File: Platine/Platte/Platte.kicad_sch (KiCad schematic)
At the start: 10 parts, among them J1 Conn_01x07_MountingPin, J2 Conn_01x04_Socket, J3 Conn_01x04_Socket

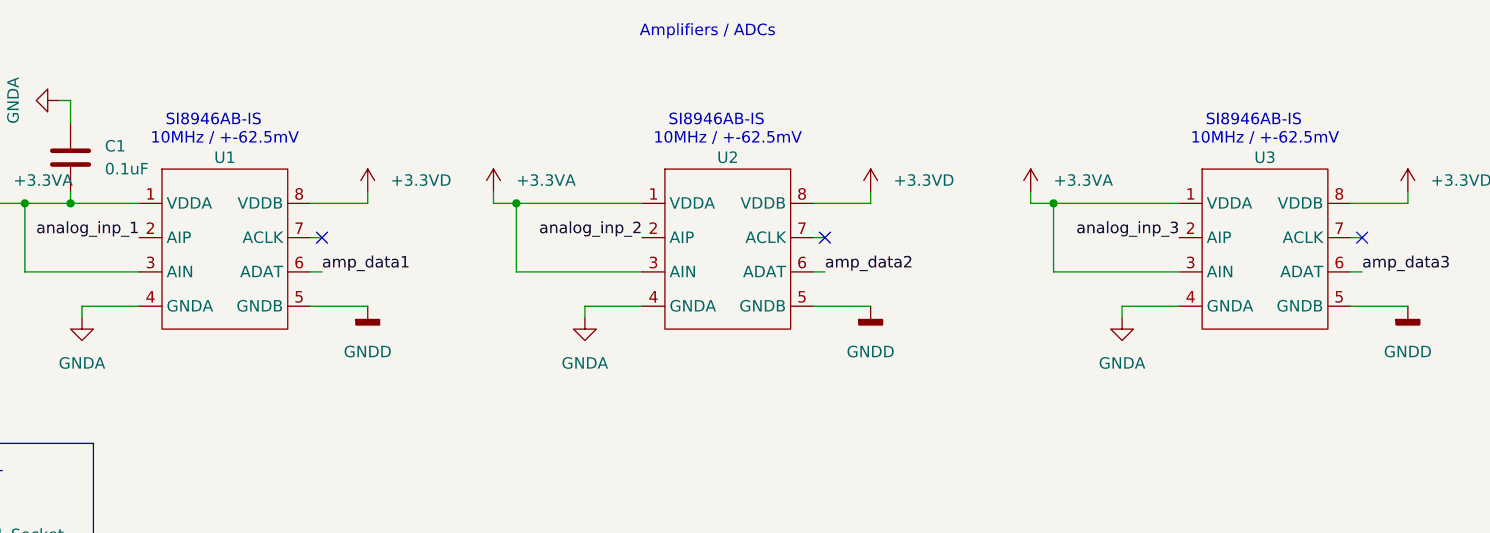
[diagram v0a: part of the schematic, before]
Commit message: Mit Robin geredet, ein paar Veränderung gemacht
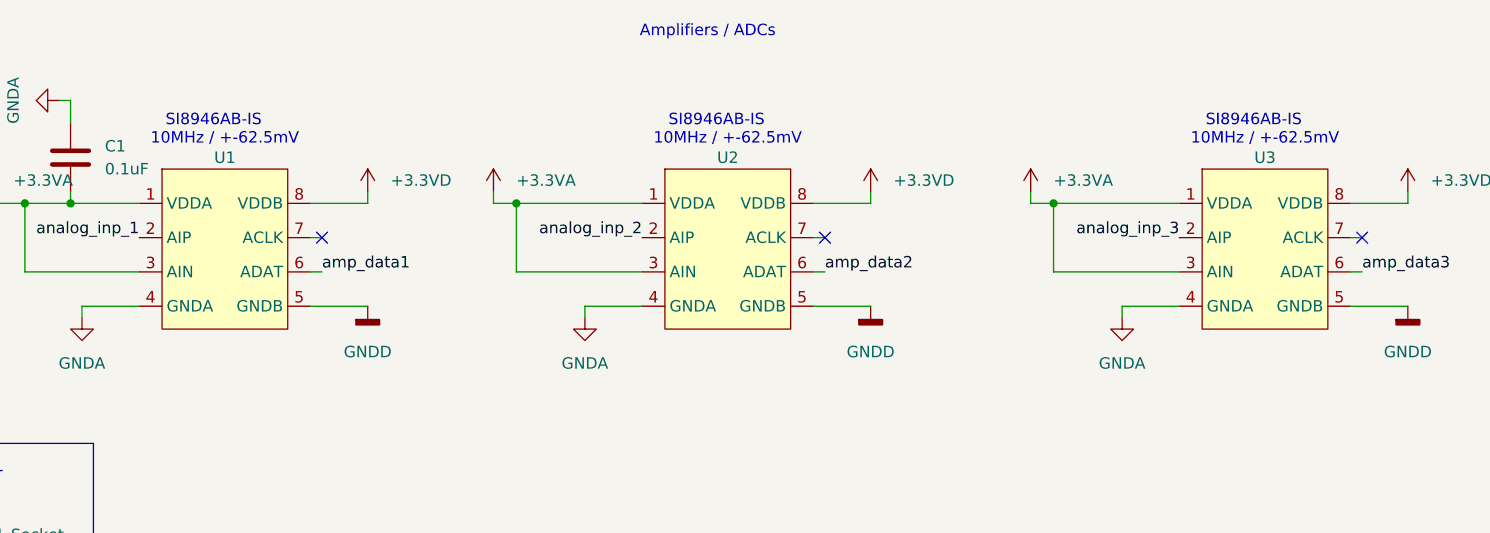
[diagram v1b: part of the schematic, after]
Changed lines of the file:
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@@
 	)
 	(symbol
+		(lib_name "_Si8941_2")
 		(lib_id "Si8941:_Si8941")
 		(at 163.83 40.64 0)
@@
 	)
 	(symbol
+		(lib_name "_Si8941_1")
 		(lib_id "Si8941:_Si8941")
 		(at 107.95 40.64 0)

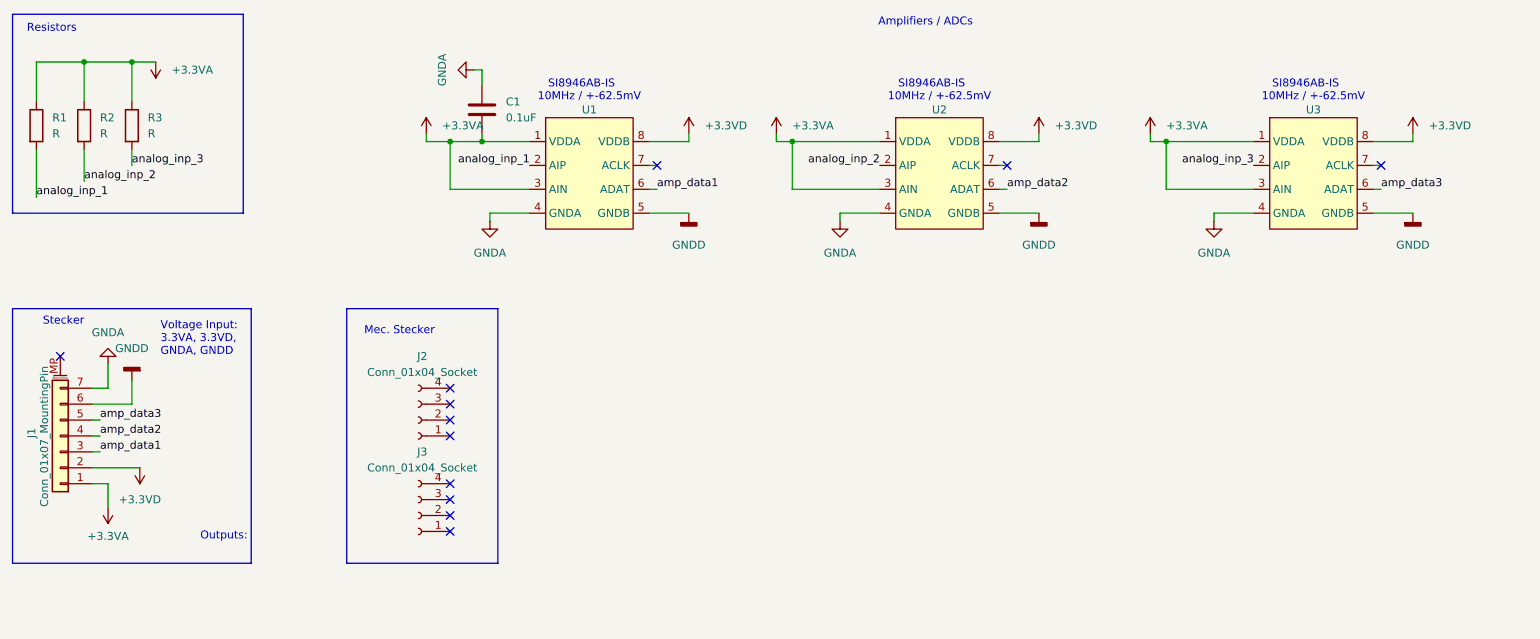
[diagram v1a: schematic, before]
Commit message: LTSpice simulation done. Changing now schematics and PCB
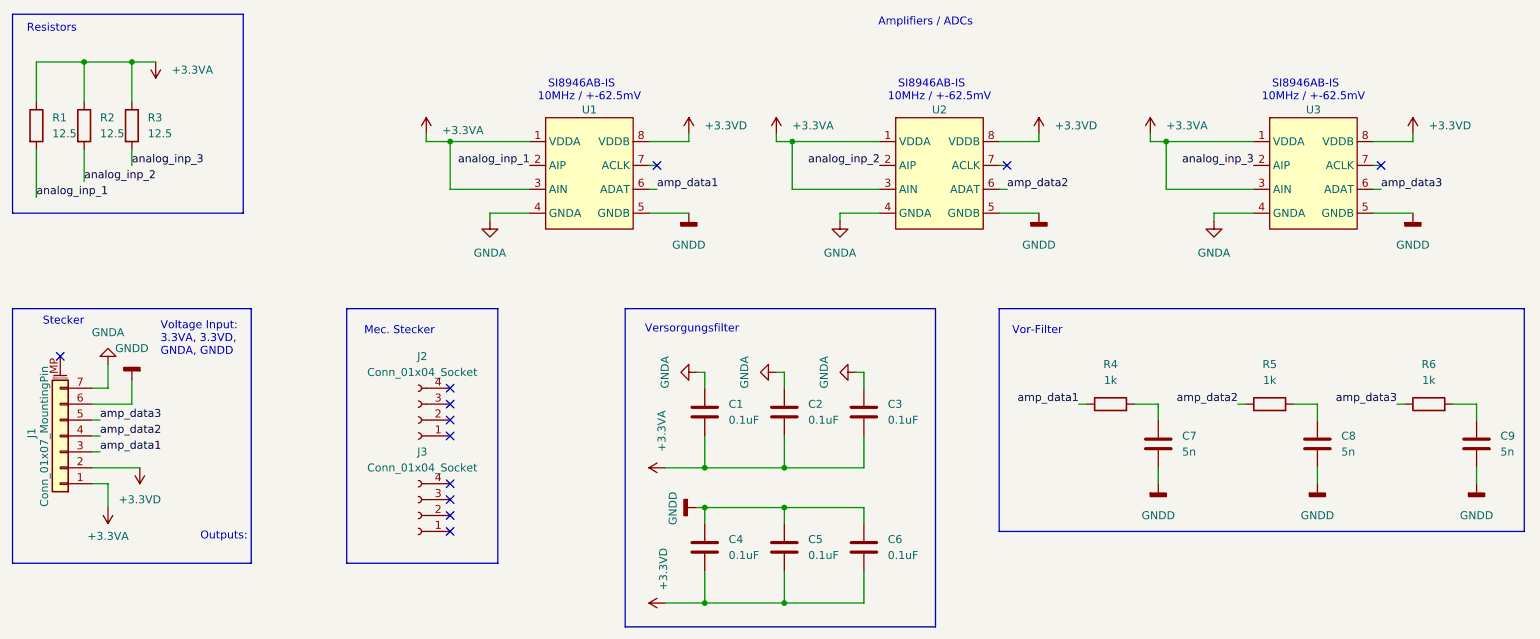
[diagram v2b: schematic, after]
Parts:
- added C2, C3, C4, C5, C6: 0.1uF, Capacitor_SMD:C_0603_1608Metric_Pad1.08x0.95mm_HandSolder, symbol Device:C
- added C7, C8, C9: 5n, Capacitor_SMD:C_0603_1608Metric_Pad1.08x0.95mm_HandSolder, symbol Device:C
- added R4, R5, R6: 1k, Resistor_SMD:R_0603_1608Metric_Pad0.98x0.95mm_HandSolder, symbol Device:R
- C1: footprint Capacitor_SMD:C_01005_0402Metric_Pad0.57x0.30mm_HandSolder -> Capacitor_SMD:C_0603_1608Metric_Pad1.08x0.95mm_HandSolder
- R1, R2, R3: value R -> 12.5; footprint Resistor_SMD:R_0201_0603Metric_Pad0.64x0.40mm_HandSolder -> Resistor_SMD:R_0603_1608Metric_Pad0.98x0.95mm_HandSolder
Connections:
- net +3.3VA: now also C2.2, C3.2
- net +3.3VD: now also C4.2, C5.2, C6.2
- net GNDA: now also C2.1, C3.1
- net GNDD: now also C4.1, C5.1, C6.1, C7.2, C8.2, C9.2
- net amp_data1: now also R4.1
- net amp_data2: now also R5.1
- net amp_data3: now also R6.1
- new net: C7.1, R4.2
- new net: C9.1, R6.2
- new net: C8.1, R5.2
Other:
- note added: "Versorgungsfilter"
- note added: "Vor-Filter"
- moved on the sheet: C1

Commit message: nicht so viel
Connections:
- net amp_data1: no longer J1.3 (Pin_3)
- net amp_data2: no longer J1.4 (Pin_4)
- net amp_data3: no longer J1.5 (Pin_5)
- net fil_da1: now reaches C7.1, R4.2
- net fil_da1: now also J1.3 (Pin_3)
- net fil_da3: now reaches C9.1, R6.2
- net fil_da3: now also J1.5 (Pin_5)
- net fil_da2: now reaches C8.1, R5.2
- net fil_da2: now also J1.4 (Pin_4)

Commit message: PCBs ready
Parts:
- removed C5, C6: 0.1uF, Capacitor_SMD:C_0603_1608Metric_Pad1.08x0.95mm_HandSolder, symbol Device:C
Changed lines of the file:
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@@
 	)
 	(junction
-		(at 127 96.52)
-		(diameter 0)
-		(color 0 0 0 0)
-	)
-	(junction
 		(at 27.94 25.4)
 		(diameter 0)
@@
 	)
 	(junction
-		(at 139.7 96.52)
-		(diameter 0)
-		(color 0 0 0 0)
-	)
-	(junction
-		(at 139.7 111.76)
-		(diameter 0)
-		(color 0 0 0 0)
-	)
-	(junction
 		(at 224.79 80.01)
 		(diameter 0)
@@
 		(color 0 0 0 0)
 	)
-	(junction
-		(at 127 111.76)
-		(diameter 0)
-		(color 0 0 0 0)
-	)
 	(no_connect
 		(at 86.36 100.33)
@@
 	(wire
 		(pts
-			(xy 152.4 111.76) (xy 152.4 106.68)
-		)
-		(stroke
-			(width 0)
-			(type default)
-		)
-	)
-	(wire
-		(pts
-			(xy 127 96.52) (xy 139.7 96.52)
-		)
-		(stroke
-			(width 0)
-			(type default)
-		)
-	)
-	(wire
-		(pts
-			(xy 139.7 111.76) (xy 152.4 111.76)
-		)
-		(stroke
-			(width 0)
-			(type default)
-		)
-	)
-	(wire
-		(pts
 			(xy 29.21 87.63) (xy 30.48 87.63)
 		)
@@
 	(wire
 		(pts
-			(xy 139.7 96.52) (xy 139.7 99.06)
-		)
-		(stroke
-			(width 0)
-			(type default)
-		)
-	)
-	(wire
-		(pts
 			(xy 29.21 85.09) (xy 30.48 85.09)
 		)
@@
 	(wire
 		(pts
-			(xy 139.7 96.52) (xy 152.4 96.52)
-		)
-		(stroke
-			(width 0)
-			(type default)
-		)
-	)
-	(wire
-		(pts
 			(xy 138.43 36.83) (xy 138.43 38.1)
 		)
@@
 	(wire
 		(pts
-			(xy 127 111.76) (xy 139.7 111.76)
-		)
-		(stroke
-			(width 0)
-			(type default)
-		)
-	)
-	(wire
-		(pts
 			(xy 208.28 49.53) (xy 208.28 50.8)
 		)
@@
 	(wire
 		(pts
-			(xy 139.7 111.76) (xy 139.7 106.68)
-		)
-		(stroke
-			(width 0)
-			(type default)
-		)
-	)
-	(wire
-		(pts
 			(xy 220.98 80.01) (xy 224.79 80.01)
 		)
@@
 	(wire
 		(pts
-			(xy 152.4 96.52) (xy 152.4 99.06)
-		)
-		(stroke
-			(width 0)
-			(type default)
-		)
-	)
-	(wire
-		(pts
 			(xy 250.19 82.55) (xy 250.19 80.01)
 		)
@@
 	)
 	(symbol
-		(lib_id "Device:C")
-		(at 152.4 102.87 0)
-		(unit 1)
-		(exclude_from_sim no)
-		(in_bom yes)
-		(on_board yes)
-		(dnp no)
-		(fields_autoplaced yes)
-		(property "Reference" "C6"
-			(at 156.21 101.5999 0)
-			(effects
-				(font
-					(size 1.27 1.27)
-				)
-				(justify left)
-			)
-		)
-		(property "Value" "0.1uF"
-			(at 156.21 104.1399 0)
-			(effects
-				(font
-					(size 1.27 1.27)
-				)
-				(justify left)
-			)
-		)
-		(property "Footprint" "Capacitor_SMD:C_0603_1608Metric_Pad1.08x0.95mm_HandSolder"
-			(at 153.3652 106.68 0)
-			(effects
-				(font
-					(size 1.27 1.27)
-				)
-				(hide yes)
-			)
-		)
-		(property "Datasheet" "~"
-			(at 152.4 102.87 0)
-			(effects
-				(font
-					(size 1.27 1.27)
-				)
-				(hide yes)
-			)
-		)
-		(property "Description" "Unpolarized capacitor"
-			(at 152.4 102.87 0)
-			(effects
-				(font
-					(size 1.27 1.27)
-				)
-				(hide yes)
-			)
-		)
-		(pin "2"
-		)
-		(pin "1"
-		)
-		(instances
-			(project "Platte"
-				(path "/8ec2d373-240e-44f6-ab9e-7e8ab23831f1"
-					(reference "C6")
-					(unit 1)
-				)
-			)
-		)
-	)
-	(symbol
 		(lib_id "Device:R")
 		(at 20.32 35.56 0)
@@
 					(unit 1)
 				)
-			)
-		)
-	)
-	(symbol
-		(lib_id "Device:C")
-		(at 139.7 102.87 0)
-		(unit 1)
-		(exclude_from_sim no)
-		(in_bom yes)
-		(on_board yes)
-		(dnp no)
-		(fields_autoplaced yes)
-		(property "Reference" "C5"
-			(at 143.51 101.5999 0)
-			(effects
-				(font
-					(size 1.27 1.27)
-				)
-				(justify left)
-			)
-		)
-		(property "Value" "0.1uF"
-			(at 143.51 104.1399 0)
-			(effects
-				(font
-					(size 1.27 1.27)
-				)
-				(justify left)
-			)
-		)
-		(property "Footprint" "Capacitor_SMD:C_0603_1608Metric_Pad1.08x0.95mm_HandSolder"
-			(at 140.6652 106.68 0)
-			(effects
-				(font
-					(size 1.27 1.27)
-				)
-				(hide yes)
-			)
-		)
-		(property "Datasheet" "~"
-			(at 139.7 102.87 0)
-			(effects
-				(font
-					(size 1.27 1.27)
-				)
-				(hide yes)
-			)
-		)
-		(property "Description" "Unpolarized capacitor"
-			(at 139.7 102.87 0)
-			(effects
-				(font
-					(size 1.27 1.27)
-				)
-				(hide yes)
-			)
-		)
-		(pin "2"
-		)
-		(pin "1"
-		)
-		(instances
-			(project "Platte"
-				(path "/8ec2d373-240e-44f6-ab9e-7e8ab23831f1"
-					(reference "C5")
-					(unit 1)
-				)

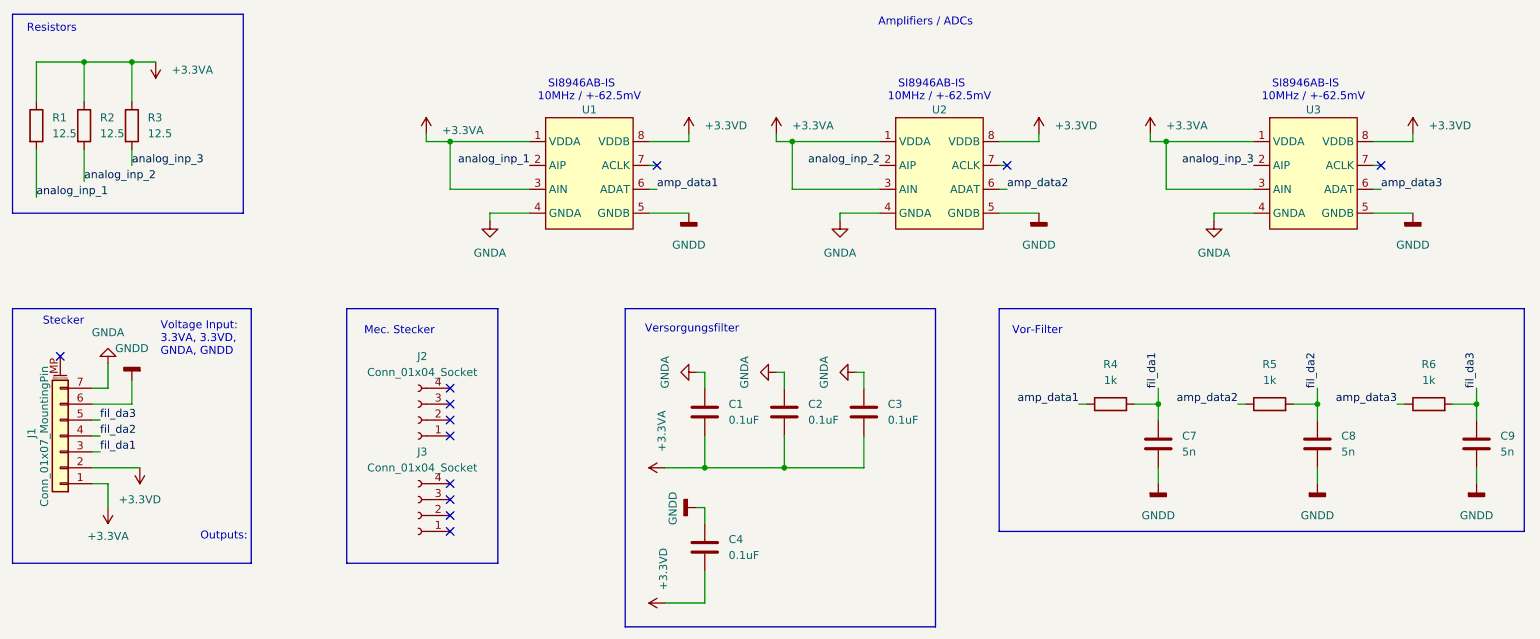
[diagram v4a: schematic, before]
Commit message: Final circuits designed. Plate PCB ready, signal cond PCB still in process
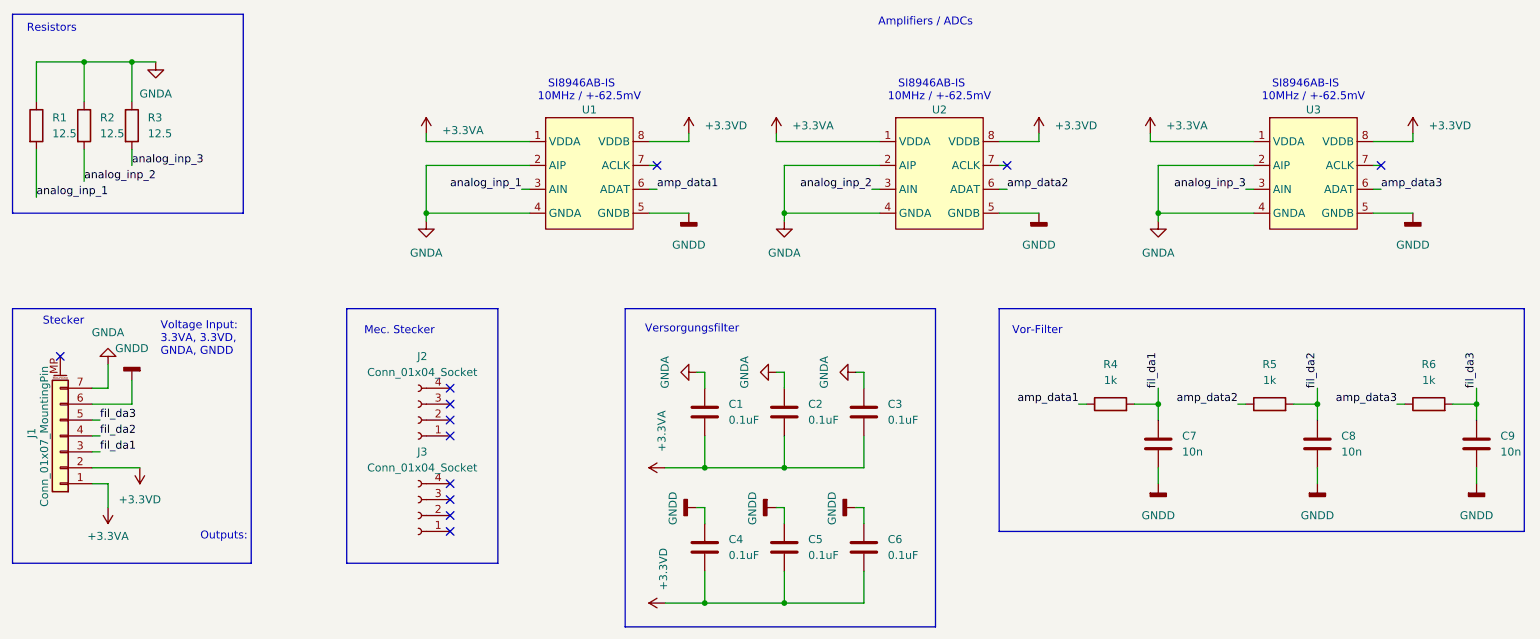
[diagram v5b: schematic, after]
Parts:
- added C5, C6: 0.1uF, Capacitor_SMD:C_0603_1608Metric_Pad1.08x0.95mm_HandSolder, symbol Device:C
- C7, C8, C9: value 5n -> 10n
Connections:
- net +3.3VA: no longer R1.1, R2.1, R3.1, U1.3 (AIN), U2.3 (AIN), U3.3 (AIN)
- net +3.3VD: now also C5.2, C6.2
- net GNDA: now also R1.1, R2.1, R3.1, U1.2 (AIP), U2.2 (AIP), U3.2 (AIP)
- net GNDD: now also C5.1, C6.1
- net analog_inp_1: now also U1.3 (AIN); no longer U1.2 (AIP)
- net analog_inp_2: now also U2.3 (AIN); no longer U2.2 (AIP)
- net analog_inp_3: now also U3.3 (AIN); no longer U3.2 (AIP)

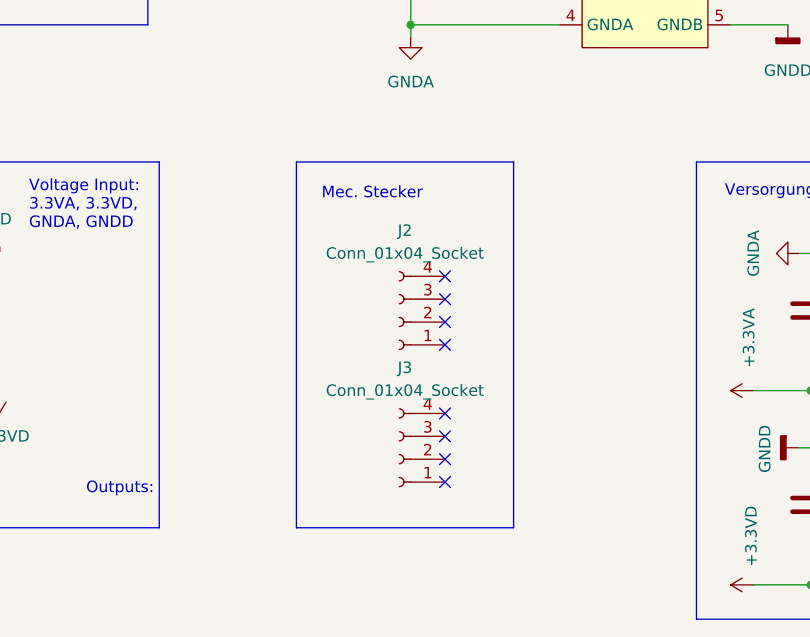
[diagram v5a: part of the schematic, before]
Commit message: Made a few changes to PCBs and schematics
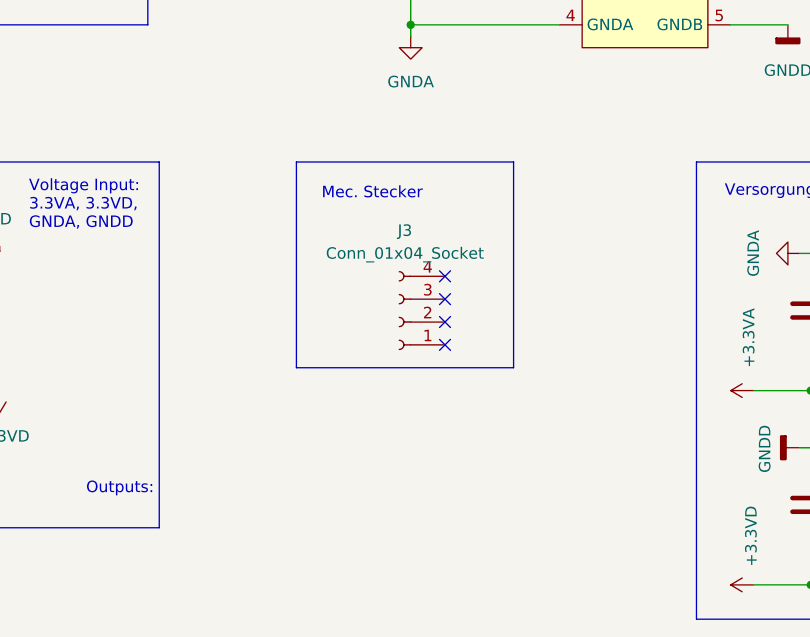
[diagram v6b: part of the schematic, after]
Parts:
- removed J2: Conn_01x04_Socket, Connector_PinHeader_1.27mm:PinHeader_1x04_P1.27mm_Vertical, symbol Connector:Conn_01x04_Socket
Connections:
- no-connect marks 12 -> 8
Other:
- moved on the sheet: J3
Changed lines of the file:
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@@
 	)
 	(no_connect
-		(at 86.36 100.33)
+		(at 86.36 85.09)
 	)
 	(no_connect
@@
 	)
 	(no_connect
-		(at 86.36 97.79)
-	)
-	(no_connect
-		(at 86.36 92.71)
-	)
-	(no_connect
-		(at 86.36 80.01)
+		(at 86.36 82.55)
 	)
 	(no_connect
@@
 	)
 	(no_connect
-		(at 86.36 85.09)
-	)
-	(no_connect
-		(at 86.36 95.25)
+		(at 86.36 80.01)
 	)
 	(no_connect
 		(at 119.38 41.91)
 	)
-	(no_connect
-		(at 86.36 82.55)
-	)
 	(wire
 		(pts
@@
 	(rectangle
 		(start 69.85 64.77)
-		(end 93.98 105.41)
+		(end 93.98 87.63)
 		(stroke
 			(width 0)
@@
 	(symbol
 		(lib_id "Connector:Conn_01x04_Socket")
-		(at 81.28 97.79 180)
+		(at 81.28 82.55 180)
 		(unit 1)
 		(exclude_from_sim no)
@@
 		(fields_autoplaced yes)
 		(property "Reference" "J3"
-			(at 81.915 87.63 0)
+			(at 81.915 72.39 0)
 			(effects
 				(font
@@
 		)
 		(property "Value" "Conn_01x04_Socket"
-			(at 81.915 90.17 0)
+			(at 81.915 74.93 0)
 			(effects
 				(font
@@
 		)
 		(property "Footprint" "Connector_PinHeader_1.27mm:PinHeader_1x04_P1.27mm_Vertical"
-			(at 81.28 97.79 0)
+			(at 81.28 82.55 0)
 			(effects
 				(font
@@
 		)
 		(property "Datasheet" "~"
-			(at 81.28 97.79 0)
+			(at 81.28 82.55 0)
 			(effects
 				(font
@@
 		)
 		(property "Description" "Generic connector, single row, 01x04, script generated"
-			(at 81.28 97.79 0)
+			(at 81.28 82.55 0)
 			(effects
 				(font
@@
 					(unit 1)
 				)
-			)
-		)
-	)
-	(symbol
-		(lib_id "Connector:Conn_01x04_Socket")
-		(at 81.28 82.55 180)
-		(unit 1)
-		(exclude_from_sim no)
-		(in_bom yes)
-		(on_board yes)
-		(dnp no)
-		(fields_autoplaced yes)
-		(property "Reference" "J2"
-			(at 81.915 72.39 0)
-			(effects
-				(font
-					(size 1.27 1.27)
-				)
-			)
-		)
-		(property "Value" "Conn_01x04_Socket"
-			(at 81.915 74.93 0)
-			(effects
-				(font
-					(size 1.27 1.27)
-				)
-			)
-		)
-		(property "Footprint" "Connector_PinHeader_1.27mm:PinHeader_1x04_P1.27mm_Vertical"
-			(at 81.28 82.55 0)
-			(effects
-				(font
-					(size 1.27 1.27)
-				)
-				(hide yes)
-			)
-		)
-		(property "Datasheet" "~"
-			(at 81.28 82.55 0)
-			(effects
-				(font
-					(size 1.27 1.27)
-				)
-				(hide yes)
-			)
-		)
-		(property "Description" "Generic connector, single row, 01x04, script generated"
-			(at 81.28 82.55 0)
-			(effects
-				(font
-					(size 1.27 1.27)
-				)
-				(hide yes)
-			)
-		)
-		(pin "2"
-		)
-		(pin "4"
-		)
-		(pin "3"
-		)
-		(pin "1"
-		)
-		(instances
-			(project ""
-				(path "/8ec2d373-240e-44f6-ab9e-7e8ab23831f1"
-					(reference "J2")
-					(unit 1)
-				)
